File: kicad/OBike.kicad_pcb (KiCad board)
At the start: 4 copper layers, 60 x 99.2 mm, 75 parts, among them J1 F34G-1A7Q1-E8C40, J2 Micro_SD_Card_Det1, J3 Conn_01x02, J4 Conn_01x04, J5 U.FL-R-SMT-1_10_, J6 Conn_01x02, J7 Conn_01x05, Q1 SS8050, Q2 SS8050, SW1 5_position_tactile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

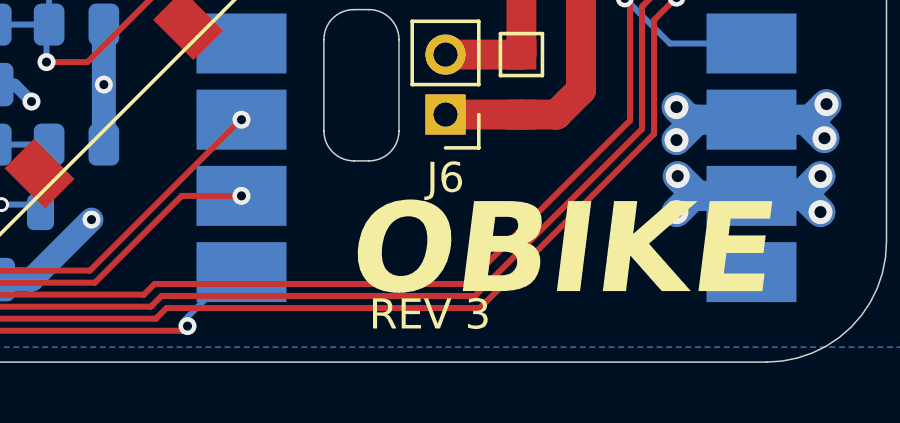
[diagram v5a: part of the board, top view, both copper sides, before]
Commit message: GPS screen nav
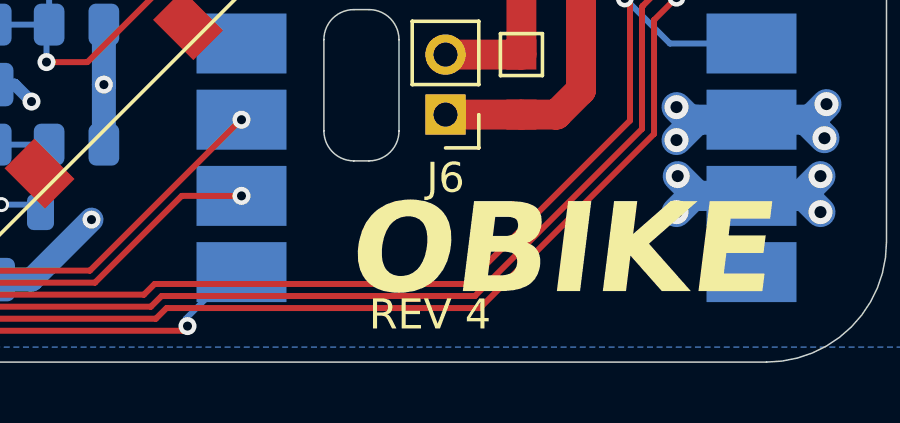
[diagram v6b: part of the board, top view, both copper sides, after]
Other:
- board text added: "REV 4"
- board text removed: "REV 3"
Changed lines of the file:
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@@
 		)
 	)
-	(gr_text "REV 3"
+	(gr_text "REV 4"
 		(at 160.8 135.25 0)
 		(layer "F.SilkS")
@@
 			(justify left bottom)
 		)
-		(render_cache "REV 3" 0
+		(render_cache "REV 4" 0
 			(polygon
 				(pts
@@
 			(polygon
 				(pts
-					(xy 164.104911 135.091723) (xy 164.049565 135.088124) (xy 164.000818 135.077824) (xy 163.957693 135.061315)
-					(xy 163.918139 135.037866) (xy 163.8845 135.008692) (xy 163.85621 134.973387) (xy 163.834318 134.933591)
-					(xy 163.817813 134.887411) (xy 163.807056 134.833803) (xy 163.949145 134.833803) (xy 163.959696 134.874651)
-					(xy 163.976647 134.905368) (xy 163.999703 134.92808) (xy 164.028413 134.944144) (xy 164.063011 134.954268)
-					(xy 164.104911 134.957878) (xy 164.149478 134.953344) (xy 164.184509 134.940801) (xy 164.212133 134.920936)
-					(xy 164.232816 134.893991) (xy 164.24576 134.859981) (xy 164.250418 134.816828) (xy 164.250418 134.786725)
-					(xy 164.245898 134.738193) (xy 164.233515 134.700527) (xy 164.214209 134.67132) (xy 164.187574 134.649193)
-					(xy 164.154109 134.635496) (xy 164.111749 134.630593) (xy 164.041346 134.630593) (xy 164.041346 134.497725)
-					(xy 164.111749 134.497725) (xy 164.149389 134.493481) (xy 164.178927 134.481681) (xy 164.202241 134.462737)
-					(xy 164.219209 134.437601) (xy 164.230047 134.405345) (xy 164.233993 134.363941) (xy 164.233993 134.333044)
-					(xy 164.229872 134.295092) (xy 164.218434 134.265284) (xy 164.200165 134.241758) (xy 164.175769 134.224491)
-					(xy 164.144443 134.21351) (xy 164.104178 134.209518) (xy 164.070203 134.212993) (xy 164.040809 134.222998)
-					(xy 164.015029 134.239438) (xy 163.99427 134.261759) (xy 163.977394 134.292541) (xy 163.964837 134.33396)
-					(xy 163.823421 134.33396) (xy 163.838152 134.273035) (xy 163.859065 134.221819) (xy 163.885712 134.178889)
-					(xy 163.918065 134.143145) (xy 163.956634 134.113997) (xy 163.999868 134.093073) (xy 164.048657 134.080164)
-					(xy 164.104178 134.075673) (xy 164.168349 134.080463) (xy 164.22166 134.09387) (xy 164.266042 134.114956)
-					(xy 164.302991 134.143511) (xy 164.332837 134.17947) (xy 164.35466 134.222311) (xy 164.368433 134.273417)
-					(xy 164.373333 134.334631) (xy 164.373333 134.351057) (xy 164.368689 134.399516) (xy 164.355222 134.442428)
-					(xy 164.333033 134.480933) (xy 164.303111 134.513868) (xy 164.265512 134.540883) (xy 164.218972 134.562083)
-					(xy 164.269925 134.578931) (xy 164.3114 134.60537) (xy 164.345001 134.641828) (xy 164.369168 134.685608)
-					(xy 164.384358 134.737954) (xy 164.389759 134.800891) (xy 164.389759 134.817316) (xy 164.384567 134.882238)
-					(xy 164.369977 134.93642) (xy 164.346866 134.981823) (xy 164.315265 135.019916) (xy 164.276165 135.050143)
-					(xy 164.229204 135.072463) (xy 164.1728 135.086654)
+					(xy 163.834351 134.926615) (xy 163.834351 134.805837) (xy 164.167742 134.087397) (xy 164.311174 134.087397)
+					(xy 163.986025 134.797655) (xy 164.473107 134.797655) (xy 164.473107 134.926615)
 				)
 			)
+			(polygon
+				(pts
+					(xy 164.262691 135.08) (xy 164.262691 134.493817) (xy 164.398613 134.493817) (xy 164.398613 135.08)
+				)
+			)

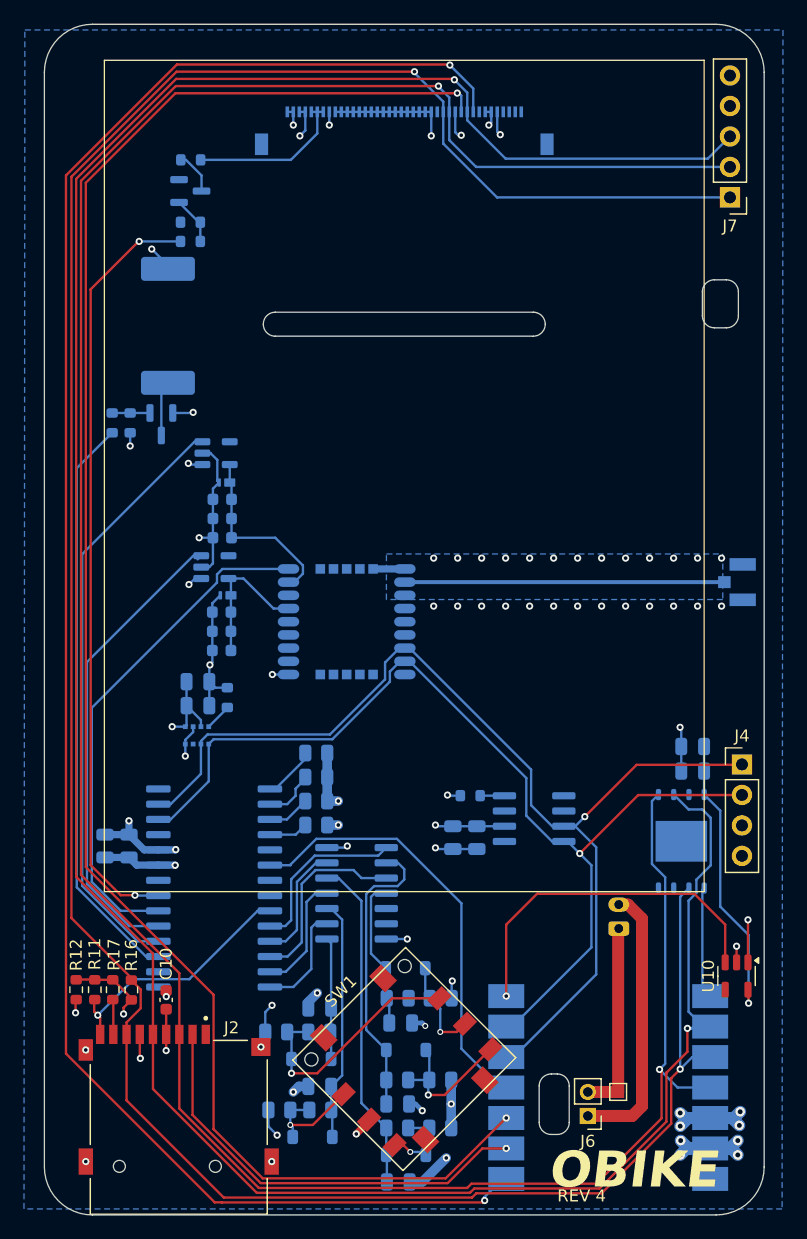
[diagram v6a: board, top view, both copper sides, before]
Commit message: PCB speaker
- buzzer now uses a header rather than SMD
- added buzzer code to HAL
- small fixes to tcx logger
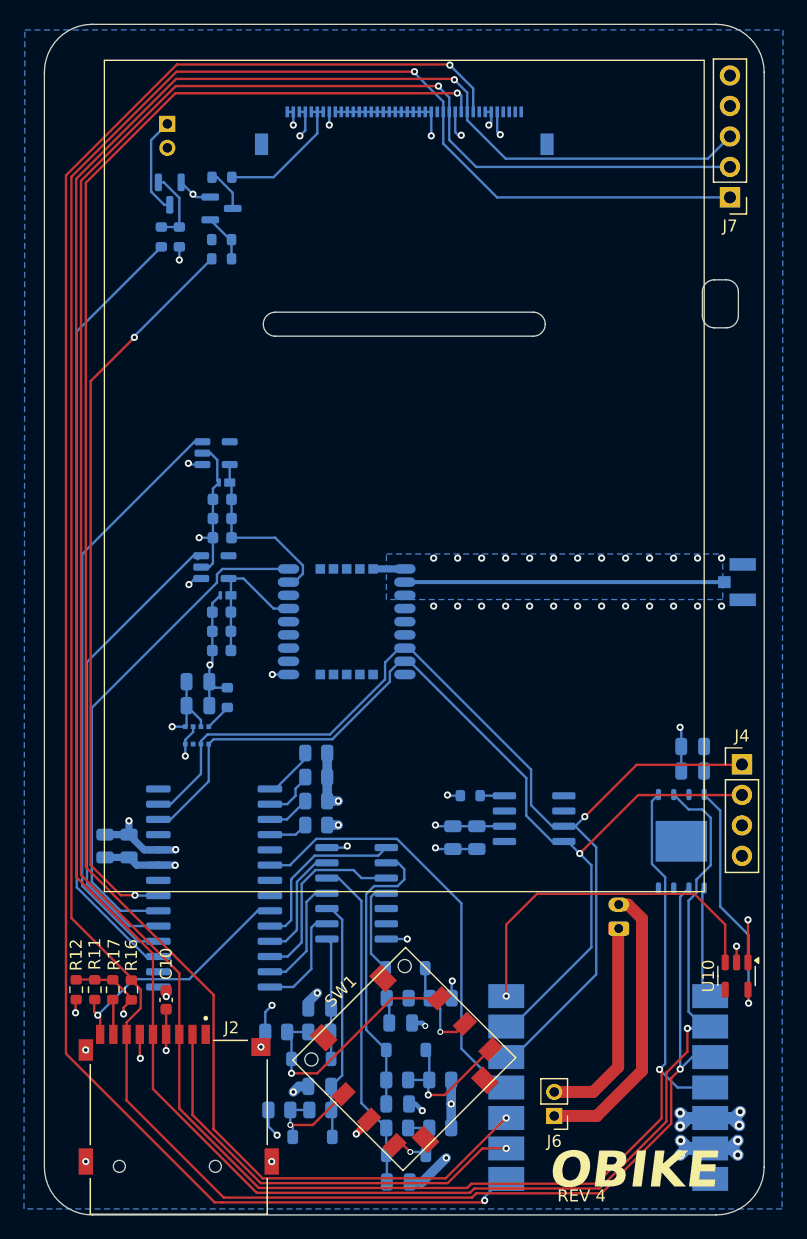
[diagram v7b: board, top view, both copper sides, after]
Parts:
- removed ?: , 
- removed LS1: ASI09N40MTRQ, Mallory:ASI09N40M
- removed REF**: TestPoint_Pad_1.0x1.0mm, TestPoint:TestPoint_Pad_1.0x1.0mm
- added J8: Conn_01x02, Connector_PinHeader_2.00mm:PinHeader_1x02_P2.00mm_Vertical, B.Cu at (128.3, 45.3)
- moved Q2 19.2 mm to (128.5, 51.1)
- moved R18 16.0 mm to (129.3, 54.7)
- moved R15 16.0 mm to (127.8, 54.7)
- moved Q1 2.98 mm to (132.8, 52.4)
- moved R36 2.98 mm to (132.8, 49.8)
- moved R37 2.98 mm to (132.8, 55.0)
- moved R38 2.98 mm to (132.8, 56.5)
- moved J6 2.80 mm to (160.6, 128.0)
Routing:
- net BUZZ: track 48.3 -> 65.6 mm
- net Net-(J8-Pin_1): track 4.48 -> 8.22 mm
- net Net-(Q2-B): track 3.15 -> 6.50 mm
- net SCR_BK: track 63.8 -> 61.4 mm
- net Net-(J1-Pad34): track 13.4 -> 11.4 mm
- net /BAT+: track 16.2 -> 17.8 mm
- net GND: track 97.4 -> 98.6 mm
- net /BAT-: track 22.9 -> 24.0 mm
- net AUX_3V3: track 243.2 -> 242.9 mm, vias 7 -> 6
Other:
- outline, holes or cut-outs redrawn

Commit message: schem updates
- added locating holes for screen to PCB
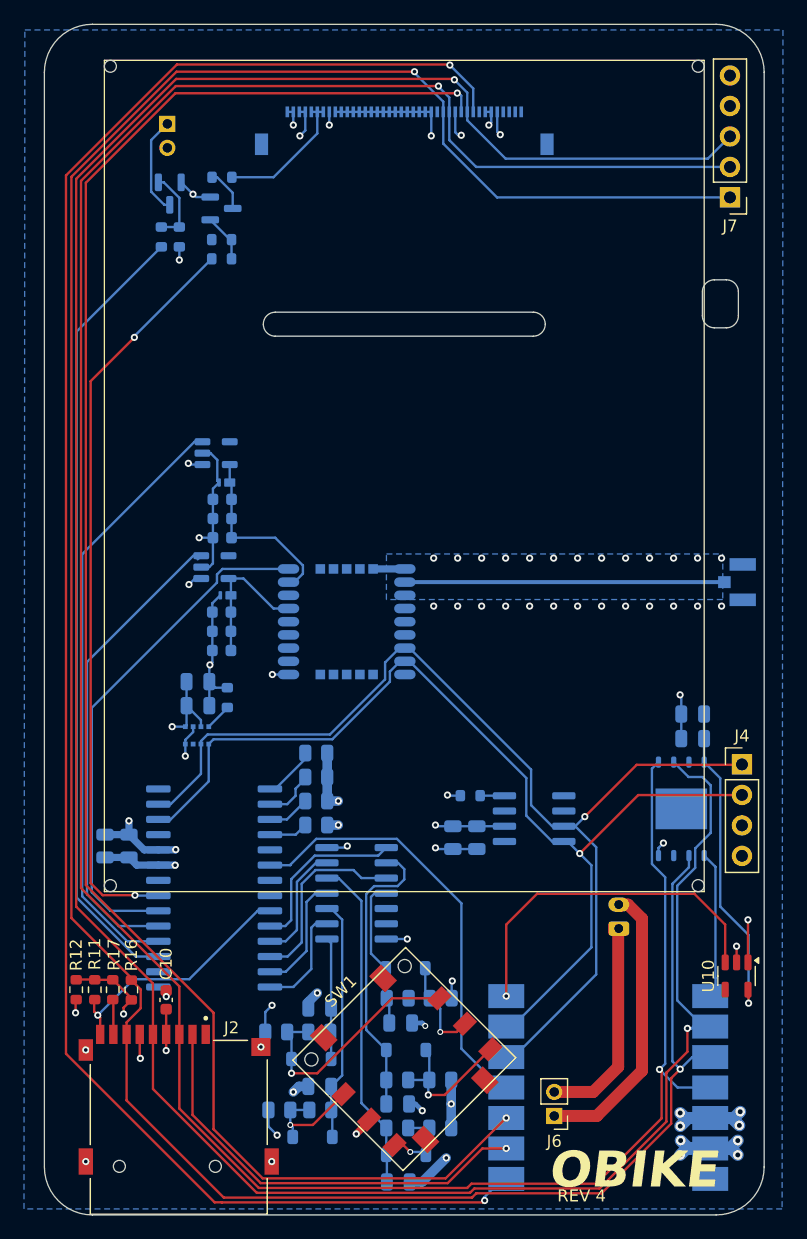
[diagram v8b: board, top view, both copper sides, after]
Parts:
- moved C13 2.70 mm to (172.1, 94.5)
- moved C14 2.70 mm to (172.1, 96.5)
- moved U9 2.70 mm to (171.1, 102.4)
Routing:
- net FL_CS: track 9.70 -> 13.2 mm
- net SCK: track 224.3 -> 227.8 mm
- net MISO: track 219.5 -> 222.7 mm
- net MOSI: track 221.1 -> 223.8 mm
- net AUX_3V3: track 242.9 -> 245.6 mm
- net GND: track 98.6 -> 99.7 mm, vias 59 -> 60
- net SCR_BK: track 61.4 -> 62.3 mm
- net GPS_BKP: track 39.5 -> 40.0 mm
- net BUZZ: track 65.6 -> 66.2 mm
- net GPS_RST: track 42.7 -> 43.2 mm
- net GPS_EN: track 49.8 -> 50.3 mm
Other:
- outline, holes or cut-outs redrawn
